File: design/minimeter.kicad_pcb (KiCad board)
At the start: 2 copper layers, 44.4 x 26.7 mm, 12 parts, among them J1 Conn_01x02_Pin, J2 I2C, SW1 SW_Push_Dual, SW2 SW_Push_Dual

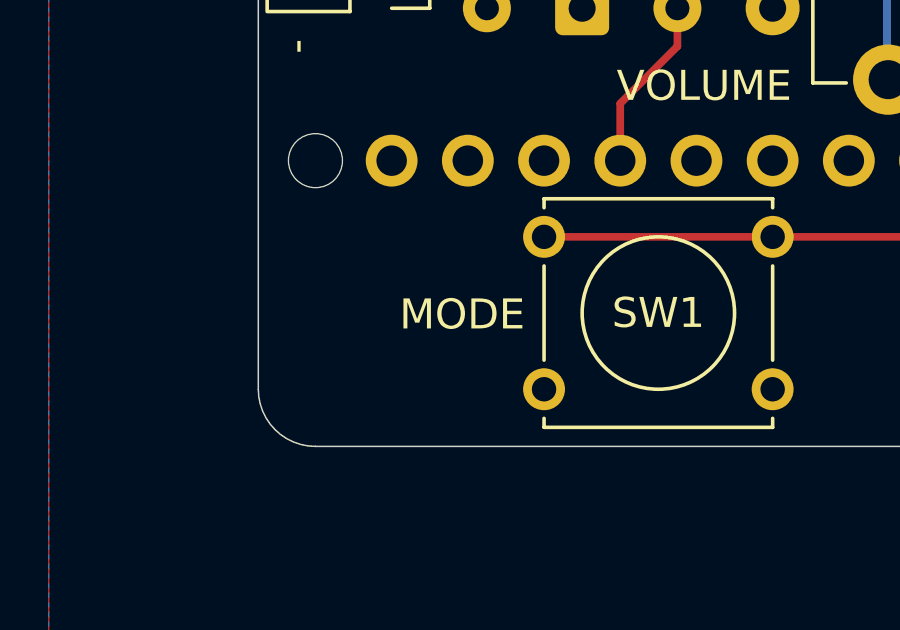
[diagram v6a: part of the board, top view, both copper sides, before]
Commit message: Update pin and button names
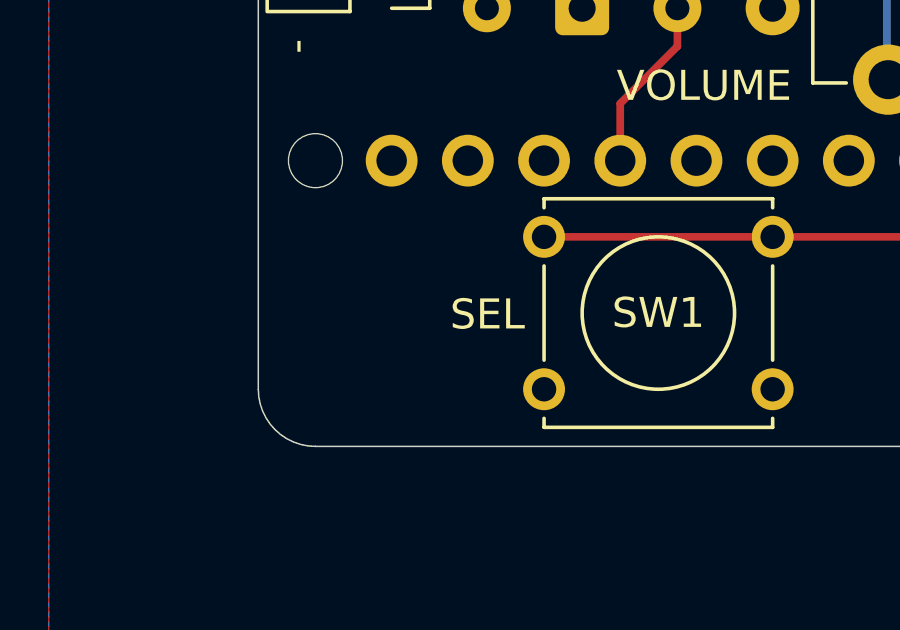
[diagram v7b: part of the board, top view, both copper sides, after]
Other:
- board text added: "SEL"
- board text removed: "MODE"
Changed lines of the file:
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@@
 		)
 	)
-	(gr_text "MODE"
+	(gr_text "SEL"
 		(at 53.975 70.485 0)
 		(layer "F.SilkS")

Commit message: Finish v2 of hardware design
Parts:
- added R3: 1K, Resistor_THT:R_Axial_DIN0207_L6.3mm_D2.5mm_P7.62mm_Horizontal, B.Cu at (57.1, 54.6)
- added R4: 220, Resistor_THT:R_Axial_DIN0207_L6.3mm_D2.5mm_P7.62mm_Horizontal, B.Cu at (57.1, 57.1)
- added R5: 220, Resistor_THT:R_Axial_DIN0207_L6.3mm_D2.5mm_P7.62mm_Horizontal, B.Cu at (57.1, 59.7)
- moved D2 10.5 mm to (52.1, 54.6)
- moved R1 9.52 mm to (47.0, 52.1), turned to 0 degrees
- moved C1 2.91 mm to (73.7, 58.4)
- moved D1 2.84 mm to (54.6, 62.2)
- moved R2 1.91 mm to (57.1, 52.1), turned to 0 degrees
- moved RV1 1.31 mm to (72.4, 62.1)
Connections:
- net /BTN_1 renamed /BTN_SEL
- net /BTN_2 renamed /BTN_OK
- net /PULL renamed /PULL_10K
- A1 pad D7: unconnected-(A1-PadD7) -> /PULL_110
- A1 pad D8: unconnected-(A1-PadD8) -> /PULL_1K
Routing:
- net /PULL_1K: track 0.00 -> 12.3 mm
- net /PULL_10K: track 5.87 -> 15.9 mm
- net /PULL_110: track 0.00 -> 8.67 mm
- net /SDA: track 31.8 -> 23.7 mm
- net /IN_PROT: track 12.6 -> 20.3 mm
- net /SPKR: track 20.5 -> 15.0 mm
- net Net-(LS1-Pad2): track 13.8 -> 12.5 mm
- net /IN: track 5.87 -> 4.86 mm
- net /SCL: track 22.0 -> 21.1 mm
- net Net-(C1-Pad2): track 4.98 -> 4.27 mm
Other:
- board text added: "MiniMeter v2 2026-01-21 Jasmine Tai"
- board text added: "← LCD"
- board text removed: "MiniMeter v1 2026-01-17 Jasmine Tai"
- board text removed: "← I²C LCD"
